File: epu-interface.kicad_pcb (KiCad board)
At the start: 2 copper layers, 69 x 100 mm, 7 parts, among them J1 SPIxxCON, J2 RJ11, J3 RJ11, J4 RJ11, J5 RJ11

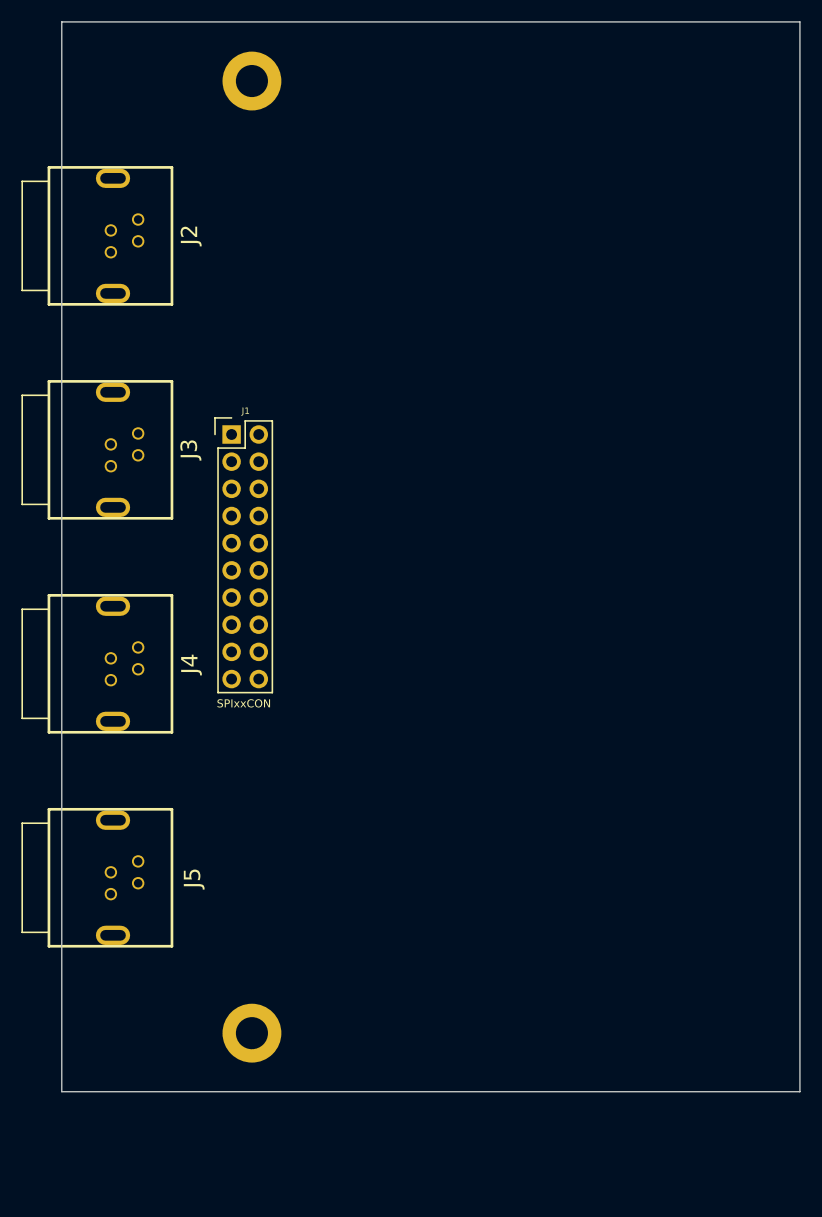
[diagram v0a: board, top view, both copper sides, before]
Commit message: Added pcb layout
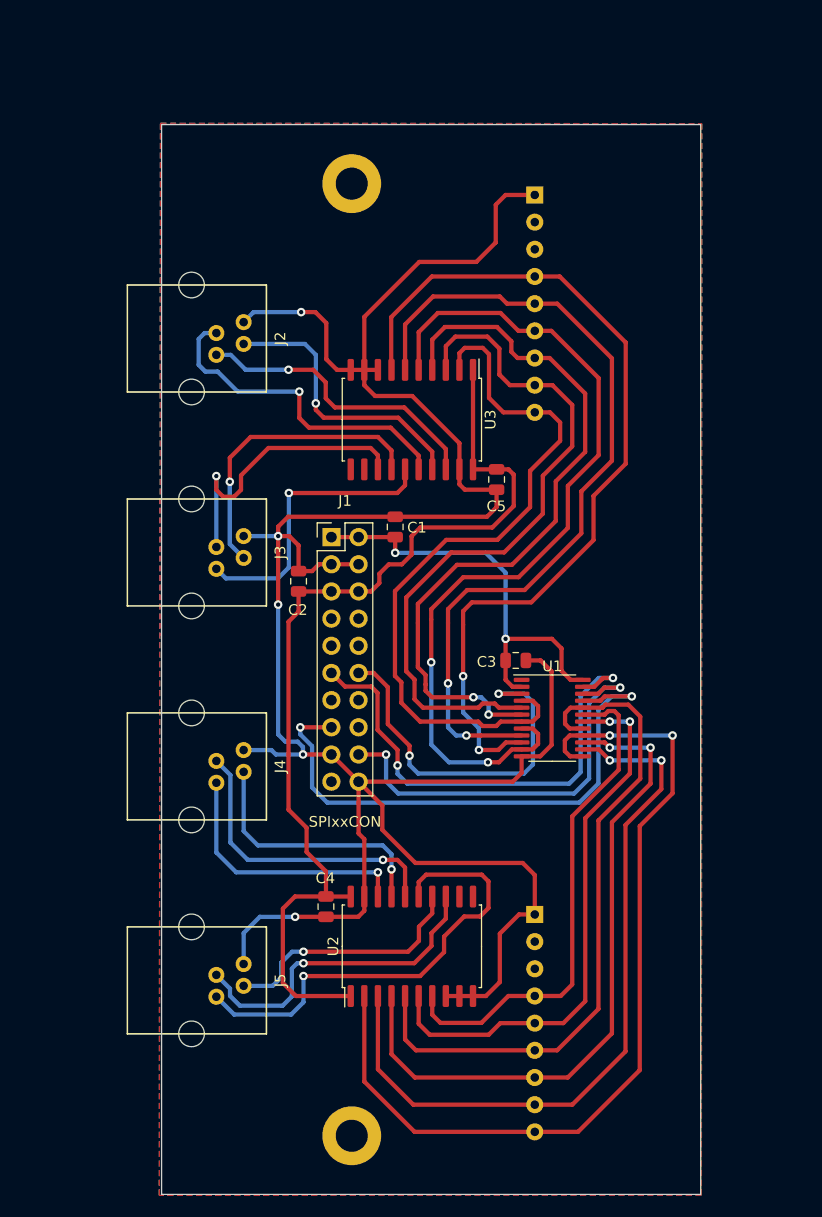
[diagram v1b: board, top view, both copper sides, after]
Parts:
- added C1: 10u, Capacitor_SMD:C_0805_2012Metric, F.Cu at (108.4, 87.0)
- added C2: 10u, Capacitor_SMD:C_0805_2012Metric, F.Cu at (99.4, 92.1)
- added C3: 100nF, Capacitor_SMD:C_0805_2012Metric, F.Cu at (119.7, 99.5)
- added C4: 100nF, Capacitor_SMD:C_0805_2012Metric, F.Cu at (102.0, 122.5)
- added C5: 100nF, Capacitor_SMD:C_0805_2012Metric, F.Cu at (117.9, 82.6)
- added RN1: 10k, Resistor_THT:R_Array_SIP9, B.Cu at (121.5, 123.3)
- added RN2: 10k, Resistor_THT:R_Array_SIP9, B.Cu at (121.5, 56.0)
- added U1: XRA1405, Package_SO:TSSOP-24_4.4x7.8mm_P0.65mm, F.Cu at (123.1, 104.9)
- added U2: 74LS245, Package_SO:SOIC-20W_7.5x12.8mm_P1.27mm, F.Cu at (110.0, 126.2)
- added U3: 74LS245, Package_SO:SOIC-20W_7.5x12.8mm_P1.27mm, F.Cu at (110.0, 77.0)
- J1: footprint Pin_Headers:Pin_Header_Straight_2x10 -> Connector_PinHeader_2.54mm:PinHeader_2x10_P2.54mm_Vertical
- J2, J3, J4, J5: footprint CONTROLE:RJ11-4P4C-HIROSE -> Controle:RJ11_2
- moved J2 16.4 mm to (89.4, 69.4)
- moved J3 16.4 mm to (89.4, 89.4)
- moved J4 16.4 mm to (89.4, 109.4)
- moved J5 16.4 mm to (89.4, 129.4)
- moved ? 13.4 mm to (104.4, 143.9)
- moved ? 13.4 mm to (104.4, 54.9)
- moved J1 13.4 mm to (102.5, 88.0)
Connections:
- net +3.3VP renamed +3V3
- J1 pad 10: /SPIxxCON/BUS_DIO2 -> unconnected-(J1-Pad10)
- J1 pad 11: /SPIxxCON/BUS_MISO -> /MISO
- J1 pad 12: /SPIxxCON/BUS_MOSI -> /MOSI
- J1 pad 13: /SPIxxCON/BUS_INTMISO -> unconnected-(J1-Pad13)
- J1 pad 14: /SPIxxCON/BUS_INTMOSI -> unconnected-(J1-Pad14)
- J1 pad 15: /SPIxxCON/BUS_CS -> /CS
- J1 pad 16: /SPIxxCON/BUS_RS -> unconnected-(J1-Pad16)
- J1 pad 18: /SPIxxCON/BUS_CLK -> /CLK
- J1 pad 19: /SPIxxCON/BUS_PwrGood -> unconnected-(J1-Pad19)
- J1 pad 7: /SPIxxCON/BUS_DIO4 -> unconnected-(J1-Pad7)
- J1 pad 8: /SPIxxCON/BUS_DIO1 -> unconnected-(J1-Pad8)
- J1 pad 9: /SPIxxCON/BUS_DIO3 -> unconnected-(J1-Pad9)
- J2 pad 1: (no net) -> /Start_A
- J2 pad 2: (no net) -> /Enable_A
- J2 pad 3: (no net) -> /Halt_A
- J2 pad 4: (no net) -> GND
- J3 pad 1: (no net) -> /Start_B
- J3 pad 2: (no net) -> /Enable_B
- J3 pad 3: (no net) -> /Halt_B
- J3 pad 4: (no net) -> GND
- J4 pad 1: (no net) -> /Start_S
- J4 pad 2: (no net) -> /Enable_S
- J4 pad 3: (no net) -> /Halt_S
- J4 pad 4: (no net) -> GND
- J5 pad 1: (no net) -> /Start_I
- J5 pad 2: (no net) -> /Enable_I
- J5 pad 3: (no net) -> /Halt_I
- J5 pad 4: (no net) -> GND
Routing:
- net GND: track 0.00 -> 233.0 mm, vias 0 -> 5
- net +5V: track 0.00 -> 92.1 mm
- net Net-(RN1-Pad9): track 0.00 -> 83.8 mm, vias 0 -> 2
- net Net-(RN2-Pad4): track 0.00 -> 83.5 mm, vias 0 -> 2
- net Net-(RN2-Pad6): track 0.00 -> 81.5 mm, vias 0 -> 2
- net Net-(RN2-Pad5): track 0.00 -> 78.2 mm, vias 0 -> 2
- net Net-(RN1-Pad8): track 0.00 -> 69.8 mm, vias 0 -> 2
- net Net-(RN2-Pad9): track 0.00 -> 68.9 mm
- net Net-(RN2-Pad7): track 0.00 -> 68.8 mm, vias 0 -> 2
- net Net-(RN2-Pad8): track 0.00 -> 66.3 mm
- net Net-(RN1-Pad6): track 0.00 -> 63.8 mm
- net Net-(RN1-Pad7): track 0.00 -> 63.4 mm, vias 0 -> 2
- net /CS: track 0.00 -> 52.4 mm, vias 0 -> 2
- net Net-(RN1-Pad5): track 0.00 -> 52.2 mm, vias 0 -> 2
- net Net-(RN1-Pad4): track 0.00 -> 47.2 mm
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- added copper zone on B.Cu, net GND
- added copper zone on F.Cu, net GND
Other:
- board size 69 x 100 mm -> 50.4 x 100 mm
- board text removed: "Colocar Apenas SMDs"
